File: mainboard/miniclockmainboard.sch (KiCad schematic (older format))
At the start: 6 parts

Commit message: Further work on the main board schematic.
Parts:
- added SW? (x2): SW_PUSH, symbol SW_PUSH
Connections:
- net GND: now also SW?.1, SW?.1
- net RXD: now also U?.5 (PIO0_4)
- net TXD: now also U?.19 (PIO0_0)
- net SSEL: now reaches U?.10 (PIO0_16)
- net SCLK: now reaches U?.11 (PIO0_15)
- net MISO: now reaches U?.12 (PIO0_1)
- net MOSI: now reaches U?.13 (XTALOUT)
- net at U?.3 (PIO0_12): now also SW?.2
- net at U?.4 (~RESET): now also SW?.2
- net SCL: now reaches U?.8 (PIO0_11)
- net SDA: now reaches U?.9 (PIO0_10)
- net +3V3 renamed VCC
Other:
- note added: "Controller"
- moved on the sheet: C?, P?, U?

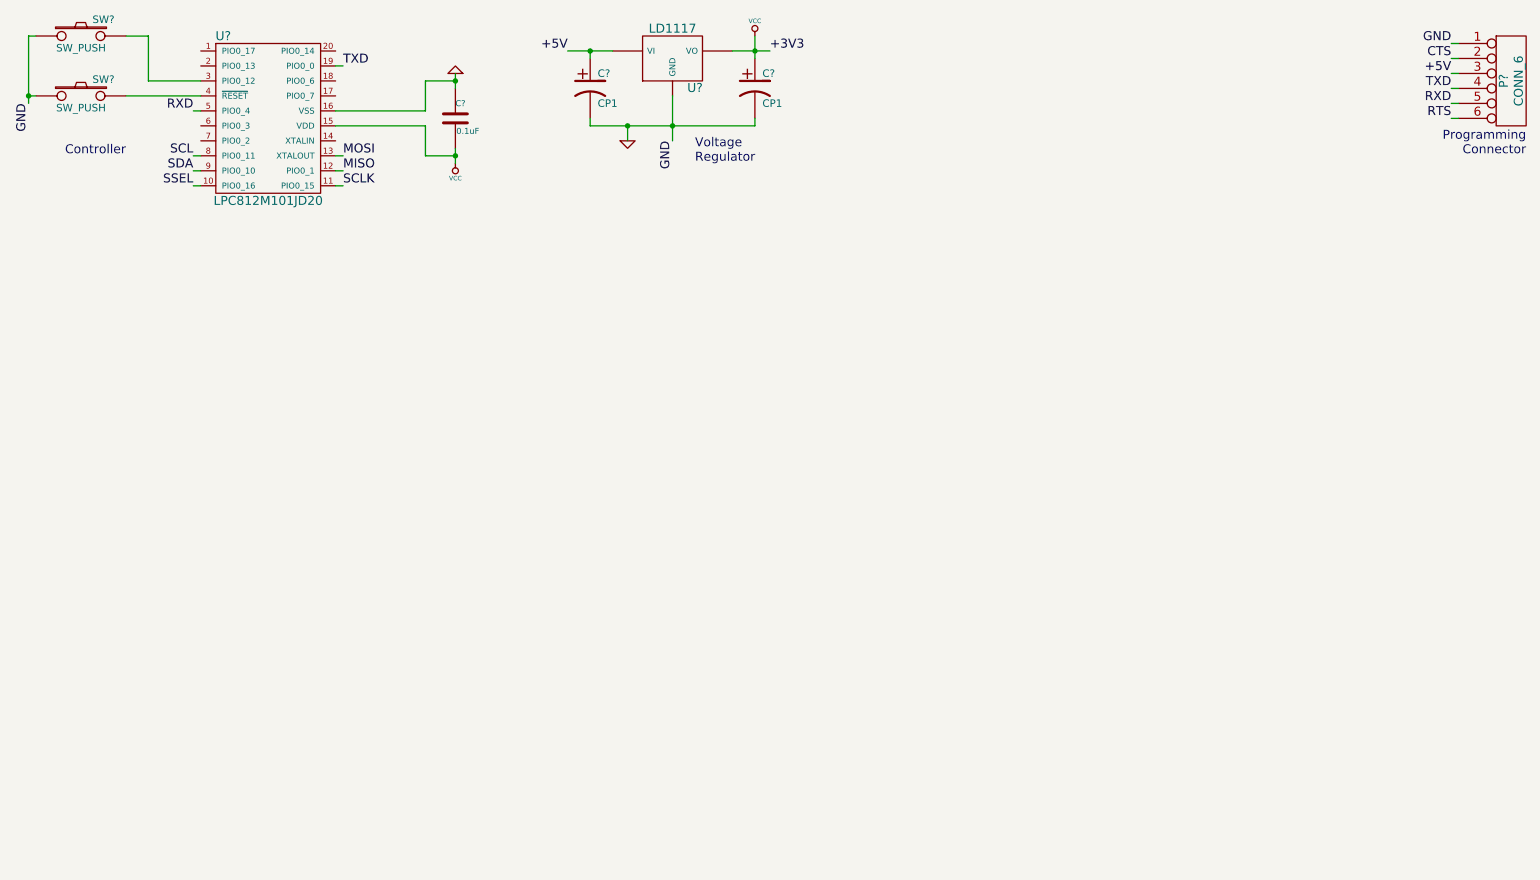
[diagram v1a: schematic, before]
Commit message: Add RTC chip, I2C/SPI headers and support bits.
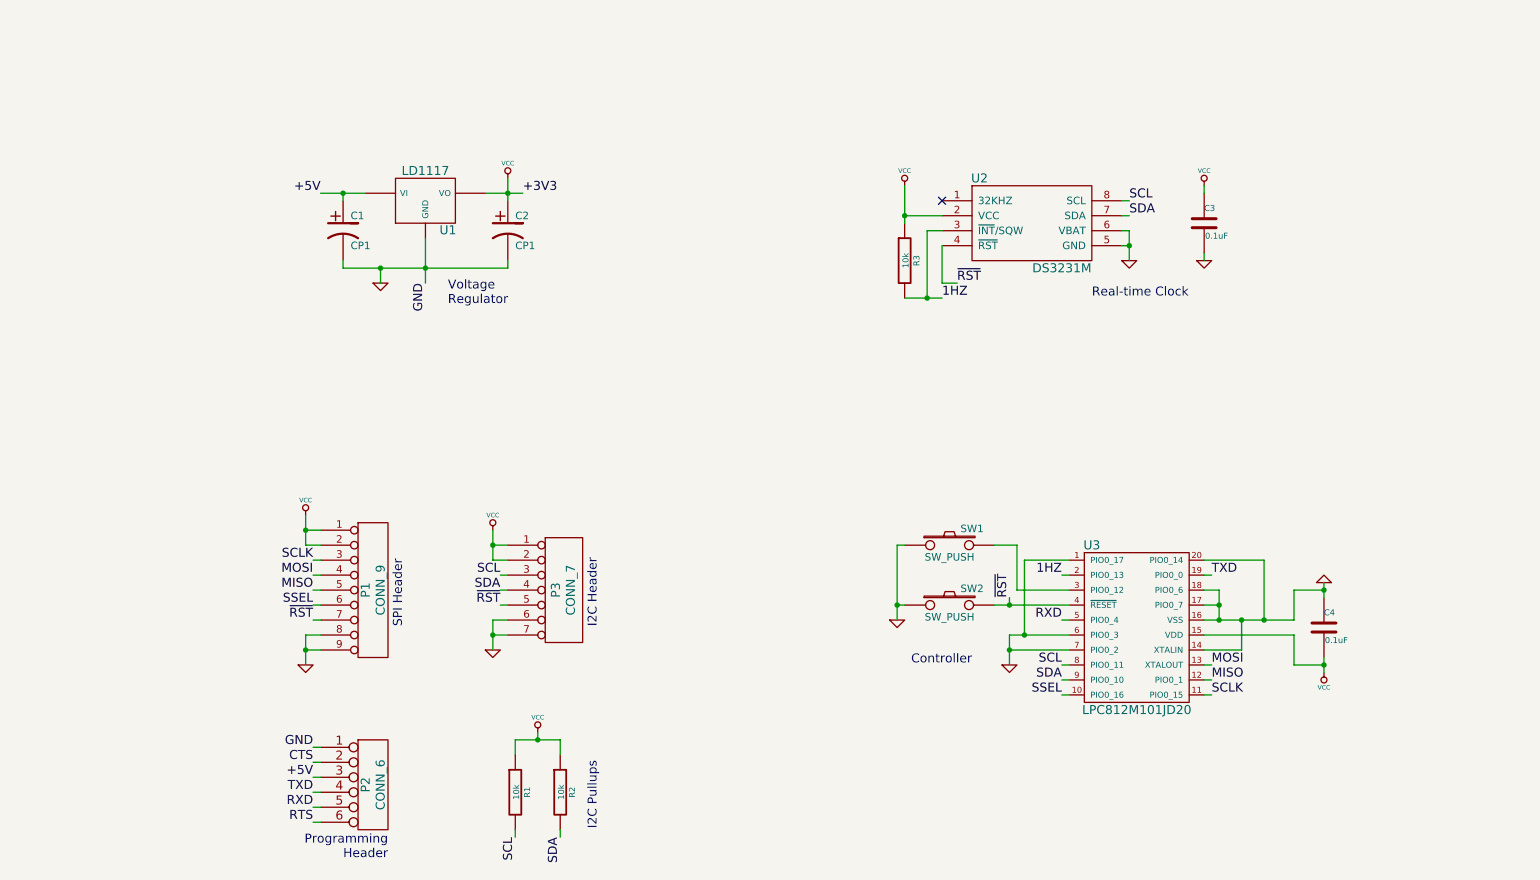
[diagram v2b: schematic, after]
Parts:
- added C3: 0.1uF, symbol C
- added P1: CONN_9, symbol CONN_9
- added P3: CONN_7, symbol CONN_7
- added R1, R2, R3: 10k, symbol R
- added U2: DS3231M, symbol DS3231M
- gave numbers to parts that had none: 8
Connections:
- net GND: now also U3.1 (PIO0_17), U3.14 (XTALIN), U3.17 (PIO0_7), U3.18 (PIO0_6), U3.20 (PIO0_14), U3.6 (PIO0_3), U3.7 (PIO0_2), C3.2, P1.8 (P8), P1.9 (P9), P3.6 (P6), P3.7 (P7), U2.5 (GND), U2.6 (VBAT)
- net MISO: now also P1.5 (P5)
- net MOSI: now also P1.4 (P4)
- net SCL: now also P3.3 (P3), R1.2, U2.8 (SCL)
- net SCLK: now also P1.3 (P3)
- net SDA: now also P3.4 (P4), R2.2, U2.7 (SDA)
- net SSEL: now also P1.6 (P6)
- net VCC: now also C3.1, P1.1 (P1), P1.2 (P2), P3.1 (P1), P3.2 (P2), R1.1, R2.1, R3.1, U2.2 (VCC)
- net 1HZ: now reaches U3.2 (PIO0_13)
- net 1HZ: now also R3.2, U2.3 (~INT~/SQW)
- net ~RST: now reaches SW2.2, U3.4 (~RESET)
- net ~RST: now also P1.7 (P7), P3.5 (P5), U2.4 (~RST)
- no-connect marks 0 -> 1
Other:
- note added: "I2C Header"
- note added: "I2C Pullups"
- note added: "Programming\nHeader"
- note added: "Real-time Clock"
- note added: "SPI Header"
- note removed: "Programming\nConnector"
- moved on the sheet: C1, C2, C4, P2, SW1, SW2, U1, U3

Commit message: Complete first rev of the main board schematic.
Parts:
- C1, C2: value CP1 -> 10uF; footprint (none) -> MiniClock:Nichicon_PolCap_6.3
- C3, C4: footprint (none) -> Capacitors_SMD:C_0805_HandSoldering
- P1: footprint (none) -> Pin_Headers:Pin_Header_Angled_1x09
- P2: footprint (none) -> Pin_Headers:Pin_Header_Angled_1x06
- P3: footprint (none) -> Pin_Headers:Pin_Header_Angled_1x07
- R1, R2, R3: footprint (none) -> Resistors_SMD:R_0805_HandSoldering
- SW1, SW2: footprint (none) -> Pin_Headers:Pin_Header_Straight_1x02
- U1: footprint (none) -> MiniClock:SOT-223
- U2: footprint (none) -> SOIC_Packages:SOIC-8_3.9x4.9mm_Pitch1.27mm
- U3: footprint (none) -> SOIC_Packages:SOIC-20_7.5x12.8mm_Pitch1.27mm
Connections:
- net GND: now also U3.10 (PIO0_16); no longer U3.14 (XTALIN)
- net MISO: now also P1.4 (P4), U3.13 (XTALOUT); no longer P1.5 (P5), U3.12 (PIO0_1)
- net MOSI: now also P1.3 (P3), U3.14 (XTALIN); no longer P1.4 (P4), U3.13 (XTALOUT)
- net SCLK: now also P1.5 (P5), U3.12 (PIO0_1); no longer P1.3 (P3), U3.11 (PIO0_15)
- net SSEL: now also U3.11 (PIO0_15); no longer U3.10 (PIO0_16)
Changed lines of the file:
@@
 F 0 "P2" V 3050 5850 60  0000 C CNN
 F 1 "CONN_6" V 3150 5850 60  0000 C CNN
-F 2 "" H 3100 5850 60  0000 C CNN
+F 2 "Pin_Headers:Pin_Header_Angled_1x06" H 3100 5850 60  0001 C CNN
 F 3 "" H 3100 5850 60  0000 C CNN
 	1    3100 5850
@@
 F 0 "U1" H 3600 1754 60  0000 C CNN
 F 1 "LD1117" H 3450 2150 60  0000 C CNN
-F 2 "" H 3450 1950 60  0000 C CNN
+F 2 "MiniClock:SOT-223" H 3450 1950 60  0001 C CNN
 F 3 "" H 3450 1950 60  0000 C CNN
 	1    3450 1950
@@
 P 4000 2150
 F 0 "C2" H 4050 2250 50  0000 L CNN
-F 1 "CP1" H 4050 2050 50  0000 L CNN
-F 2 "" H 4000 2150 60  0000 C CNN
+F 1 "10uF" H 4050 2050 50  0000 L CNN
+F 2 "MiniClock:Nichicon_PolCap_6.3" H 4000 2150 60  0001 C CNN
 F 3 "" H 4000 2150 60  0000 C CNN
 	1    4000 2150
@@
 P 2900 2150
 F 0 "C1" H 2950 2250 50  0000 L CNN
-F 1 "CP1" H 2950 2050 50  0000 L CNN
-F 2 "" H 2900 2150 60  0000 C CNN
+F 1 "10uF" H 2950 2050 50  0000 L CNN
+F 2 "MiniClock:Nichicon_PolCap_6.3" H 2900 2150 60  0001 C CNN
 F 3 "" H 2900 2150 60  0000 C CNN
 	1    2900 2150
@@
 F 0 "U3" H 7900 5350 60  0000 C CNN
 F 1 "LPC812M101JD20" H 8200 4250 60  0000 C CNN
-F 2 "" H 8200 5000 60  0000 C CNN
+F 2 "SOIC_Packages:SOIC-20_7.5x12.8mm_Pitch1.27mm" H 8200 5000 60  0001 C CNN
 F 3 "" H 8200 5000 60  0000 C CNN
 	1    8200 4800
@@
 F 0 "C4" H 9450 4900 40  0000 L CNN
 F 1 "0.1uF" H 9456 4715 40  0000 L CNN
-F 2 "" H 9488 4650 30  0000 C CNN
+F 2 "Capacitors_SMD:C_0805_HandSoldering" H 9488 4650 30  0001 C CNN
 F 3 "" H 9450 4800 60  0000 C CNN
 	1    9450 4800
@@
 F 0 "SW1" H 7100 4360 50  0000 C CNN
 F 1 "SW_PUSH" H 6950 4170 50  0000 C CNN
-F 2 "" H 6950 4250 60  0000 C CNN
+F 2 "Pin_Headers:Pin_Header_Straight_1x02" H 6950 4250 60  0001 C CNN
 F 3 "" H 6950 4250 60  0000 C CNN
 	1    6950 4250
@@
 F 0 "SW2" H 7100 4760 50  0000 C CNN
 F 1 "SW_PUSH" H 6950 4570 50  0000 C CNN
-F 2 "" H 6950 4650 60  0000 C CNN
+F 2 "Pin_Headers:Pin_Header_Straight_1x02" H 6950 4650 60  0001 C CNN
 F 3 "" H 6950 4650 60  0000 C CNN
 	1    6950 4650
@@
 Text Label 7700 5150 2    60   ~ 0
 SDA
+Text Label 8700 5150 0    60   ~ 0
+SCLK
+Text Label 8700 4950 0    60   ~ 0
+MOSI
+Text Label 8700 5050 0    60   ~ 0
+MISO
 Text Label 8700 5250 0    60   ~ 0
-SCLK
-Text Label 8700 5050 0    60   ~ 0
-MOSI
-Text Label 8700 5150 0    60   ~ 0
-MISO
-Text Label 7700 5250 2    60   ~ 0
 SSEL
 Wire Wire Line
-	8650 5050 8700 5050
-Wire Wire Line
-	8650 5150 8700 5150
-Wire Wire Line
-	8650 5250 8700 5250
-Wire Wire Line
 	8650 4450 8700 4450
 Wire Wire Line
@@
 Wire Wire Line
 	7700 5150 7750 5150
-Wire Wire Line
-	7700 5250 7750 5250
-$Comp
-L GND #PWR3
+$Comp
+L GND #PWR01
 U 1 1 5516F441
 P 3150 2500
-F 0 "#PWR3" H 3150 2500 30  0001 C CNN
+F 0 "#PWR01" H 3150 2500 30  0001 C CNN
 F 1 "GND" H 3150 2430 30  0001 C CNN
 F 2 "" H 3150 2500 60  0000 C CNN
@@
 Connection ~ 3150 2400
 $Comp
-L VCC #PWR6
+L VCC #PWR02
 U 1 1 5516F505
 P 4000 1800
-F 0 "#PWR6" H 4000 1900 30  0001 C CNN
+F 0 "#PWR02" H 4000 1900 30  0001 C CNN
 F 1 "VCC" H 4000 1900 30  0000 C CNN
 F 2 "" H 4000 1800 60  0000 C CNN
@@
 $EndComp
 $Comp
-L VCC #PWR15
+L VCC #PWR03
 U 1 1 5516F5B2
 P 9450 5100
-F 0 "#PWR15" H 9450 5200 30  0001 C CNN
+F 0 "#PWR03" H 9450 5200 30  0001 C CNN
 F 1 "VCC" H 9450 5200 30  0000 C CNN
 F 2 "" H 9450 5100 60  0000 C CNN
@@
 	9450 5000 9450 5100
 $Comp
-L GND #PWR14
+L GND #PWR04
 U 1 1 5516F6A7
 P 9450 4500
-F 0 "#PWR14" H 9450 4500 30  0001 C CNN
+F 0 "#PWR04" H 9450 4500 30  0001 C CNN
 F 1 "GND" H 9450 4430 30  0001 C CNN
 F 2 "" H 9450 4500 60  0000 C CNN
@@
 F 0 "U2" H 7150 2400 60  0000 C CNN
 F 1 "DS3231M" H 7700 1800 60  0000 C CNN
-F 2 "" H 7500 2050 60  0000 C CNN
+F 2 "SOIC_Packages:SOIC-8_3.9x4.9mm_Pitch1.27mm" H 7500 2050 60  0001 C CNN
 F 3 "" H 7500 2050 60  0000 C CNN
 	1    7500 2100
@@
 $EndComp
 $Comp
-L GND #PWR11
+L GND #PWR05
 U 1 1 55170758
 P 8150 2350
-F 0 "#PWR11" H 8150 2350 30  0001 C CNN
+F 0 "#PWR05" H 8150 2350 30  0001 C CNN
 F 1 "GND" H 8150 2280 30  0001 C CNN
 F 2 "" H 8150 2350 60  0000 C CNN
@@
 Connection ~ 8150 2250
 $Comp
-L VCC #PWR9
+L VCC #PWR06
 U 1 1 55170815
 P 6650 1850
-F 0 "#PWR9" H 6650 1950 30  0001 C CNN
+F 0 "#PWR06" H 6650 1950 30  0001 C CNN
 F 1 "VCC" H 6650 1950 30  0000 C CNN
 F 2 "" H 6650 1850 60  0000 C CNN
@@
 	6650 1850 6650 2100
 $Comp
-L VCC #PWR12
+L VCC #PWR07
 U 1 1 5517086E
 P 8650 1850
-F 0 "#PWR12" H 8650 1950 30  0001 C CNN
+F 0 "#PWR07" H 8650 1950 30  0001 C CNN
 F 1 "VCC" H 8650 1950 30  0000 C CNN
 F 2 "" H 8650 1850 60  0000 C CNN
@@
 $EndComp
 $Comp
-L GND #PWR13
+L GND #PWR08
 U 1 1 5517088B
 P 8650 2350
-F 0 "#PWR13" H 8650 2350 30  0001 C CNN
+F 0 "#PWR08" H 8650 2350 30  0001 C CNN
 F 1 "GND" H 8650 2280 30  0001 C CNN
 F 2 "" H 8650 2350 60  0000 C CNN
@@
 F 0 "C3" H 8650 2200 40  0000 L CNN
 F 1 "0.1uF" H 8656 2015 40  0000 L CNN
-F 2 "" H 8688 1950 30  0000 C CNN
+F 2 "Capacitors_SMD:C_0805_HandSoldering" H 8688 1950 30  0001 C CNN
 F 3 "" H 8650 2100 60  0000 C CNN
 	1    8650 2100
@@
 F 0 "R3" V 6730 2350 40  0000 C CNN
 F 1 "10k" V 6657 2351 40  0000 C CNN
-F 2 "" V 6580 2350 30  0000 C CNN
+F 2 "Resistors_SMD:R_0805_HandSoldering" V 6580 2350 30  0001 C CNN
 F 3 "" H 6650 2350 30  0000 C CNN
 	1    6650 2350
@@
 	6900 2500 7000 2500
 $Comp
-L VCC #PWR7
+L VCC #PWR09
 U 1 1 551715D8
 P 4200 5500
-F 0 "#PWR7" H 4200 5600 30  0001 C CNN
+F 0 "#PWR09" H 4200 5600 30  0001 C CNN
 F 1 "VCC" H 4200 5600 30  0000 C CNN
 F 2 "" H 4200 5500 60  0000 C CNN
@@
 F 0 "R1" V 4130 5900 40  0000 C CNN
 F 1 "10k" V 4057 5901 40  0000 C CNN
-F 2 "" V 3980 5900 30  0000 C CNN
+F 2 "Resistors_SMD:R_0805_HandSoldering" V 3980 5900 30  0001 C CNN
 F 3 "" H 4050 5900 30  0000 C CNN
 	1    4050 5900
@@
 F 0 "R2" V 4430 5900 40  0000 C CNN
 F 1 "10k" V 4357 5901 40  0000 C CNN
-F 2 "" V 4280 5900 30  0000 C CNN
+F 2 "Resistors_SMD:R_0805_HandSoldering" V 4280 5900 30  0001 C CNN
 F 3 "" H 4350 5900 30  0000 C CNN
 	1    4350 5900
@@
 Text Notes 4600 6150 1    60   ~ 0
 I2C Pullups
+Text Label 2700 4550 2    60   ~ 0
+SCLK
 Text Label 2700 4350 2    60   ~ 0
-SCLK
+MOSI
 Text Label 2700 4450 2    60   ~ 0
-MOSI
-Text Label 2700 4550 2    60   ~ 0
 MISO
 Text Label 2700 4650 2    60   ~ 0
 SSEL
 $Comp
-L GND #PWR2
+L GND #PWR010
 U 1 1 55172A4F
 P 2650 5050
-F 0 "#PWR2" H 2650 5050 30  0001 C CNN
+F 0 "#PWR010" H 2650 5050 30  0001 C CNN
 F 1 "GND" H 2650 4980 30  0001 C CNN
 F 2 "" H 2650 5050 60  0000 C CNN
@@
 $EndComp
 $Comp
-L VCC #PWR1
+L VCC #PWR011
 U 1 1 55172A71
 P 2650 4050
-F 0 "#PWR1" H 2650 4150 30  0001 C CNN
+F 0 "#PWR011" H 2650 4150 30  0001 C CNN
 F 1 "VCC" H 2650 4150 30  0000 C CNN
 F 2 "" H 2650 4050 60  0000 C CNN
@@
 F 0 "P1" V 3050 4550 60  0000 C CNN
 F 1 "CONN_9" V 3150 4550 60  0000 C CNN
-F 2 "" H 3100 4550 60  0000 C CNN
+F 2 "Pin_Headers:Pin_Header_Angled_1x09" H 3100 4550 60  0001 C CNN
 F 3 "" H 3100 4550 60  0000 C CNN
 	1    3100 4550
@@
 Wire Wire Line
 	2650 4950 2750 4950
-Wire Wire Line
-	2700 4350 2750 4350
-Wire Wire Line
-	2700 4450 2750 4450
-Wire Wire Line
-	2700 4550 2750 4550
 Wire Wire Line
 	2700 4650 2750 4650
@@
 F 0 "P3" V 4320 4550 60  0000 C CNN
 F 1 "CONN_7" V 4420 4550 60  0000 C CNN
-F 2 "" H 4350 4550 60  0000 C CNN
+F 2 "Pin_Headers:Pin_Header_Angled_1x07" H 4350 4550 60  0001 C CNN
 F 3 "" H 4350 4550 60  0000 C CNN
 	1    4350 4550
@@
 $EndComp
 $Comp
-L GND #PWR5
+L GND #PWR012
 U 1 1 5517329D
 P 3900 4950
-F 0 "#PWR5" H 3900 4950 30  0001 C CNN
+F 0 "#PWR012" H 3900 4950 30  0001 C CNN
 F 1 "GND" H 3900 4880 30  0001 C CNN
 F 2 "" H 3900 4950 60  0000 C CNN
@@
 $EndComp
 $Comp
-L VCC #PWR4
+L VCC #PWR013
 U 1 1 551732C0
 P 3900 4150
-F 0 "#PWR4" H 3900 4250 30  0001 C CNN
+F 0 "#PWR013" H 3900 4250 30  0001 C CNN
 F 1 "VCC" H 3900 4250 30  0000 C CNN
 F 2 "" H 3900 4150 60  0000 C CNN
@@
 Wire Wire Line
 	8650 4350 9050 4350
-Wire Wire Line
-	8650 4950 8900 4950
-$Comp
-L GND #PWR8
+$Comp
+L GND #PWR014
 U 1 1 551768E3
 P 6600 4750
-F 0 "#PWR8" H 6600 4750 30  0001 C CNN
+F 0 "#PWR014" H 6600 4750 30  0001 C CNN
 F 1 "GND" H 6600 4680 30  0001 C CNN
 F 2 "" H 6600 4750 60  0000 C CNN
@@
 Connection ~ 7350 4650
 $Comp
-L GND #PWR10
+L GND #PWR015
 U 1 1 55176A63
-P 7350 5050
-F 0 "#PWR10" H 7350 5050 30  0001 C CNN
-F 1 "GND" H 7350 4980 30  0001 C CNN
-F 2 "" H 7350 5050 60  0000 C CNN
-F 3 "" H 7350 5050 60  0000 C CNN
-	1    7350 5050
-	1    0    0    -1
-$EndComp
-Wire Wire Line
-	7350 5050 7350 4850
-Wire Wire Line
-	7350 4850 7750 4850
+P 7350 5350
+F 0 "#PWR015" H 7350 5350 30  0001 C CNN
+F 1 "GND" H 7350 5280 30  0001 C CNN
+F 2 "" H 7350 5350 60  0000 C CNN
+F 3 "" H 7350 5350 60  0000 C CNN
+	1    7350 5350
+	1    0    0    -1
+$EndComp
 Wire Wire Line
 	7750 4950 7350 4950
-Connection ~ 7350 4950
 Wire Wire Line
 	7750 4350 7450 4350
 Wire Wire Line
-	7450 4350 7450 4850
-Connection ~ 7450 4850
+	7450 4350 7450 4950
 Wire Wire Line
 	8750 4550 8750 4750
@@
 Connection ~ 9050 4750
 Wire Wire Line
-	8900 4950 8900 4750
-Connection ~ 8900 4750
+	2700 4350 2750 4350
+Wire Wire Line
+	2700 4450 2750 4450
+Wire Wire Line
+	2700 4550 2750 4550
+Wire Wire Line
+	8650 4950 8700 4950
+Wire Wire Line
+	8650 5050 8700 5050
+Wire Wire Line
+	8650 5150 8700 5150
+Wire Wire Line
+	8650 5250 8700 5250
+Wire Wire Line
+	7350 4950 7350 5350
+Wire Wire Line
+	7750 5250 7350 5250
+Connection ~ 7350 5250
+Wire Wire Line
+	7450 4850 7750 4850
+Connection ~ 7450 4850
+Connection ~ 7450 4950
 $EndSCHEMATC
